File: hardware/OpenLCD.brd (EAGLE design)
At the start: 45.7 x 30.5 mm, 42 parts, among them Q1 PNP-500mA, Q2 PNP-500mA, Q3 PNP-500mA, U1 ATMEGA328P_TQFP, U2 4BIT-RGB, U3 MIC5205-ADJ, Y2 8MHz

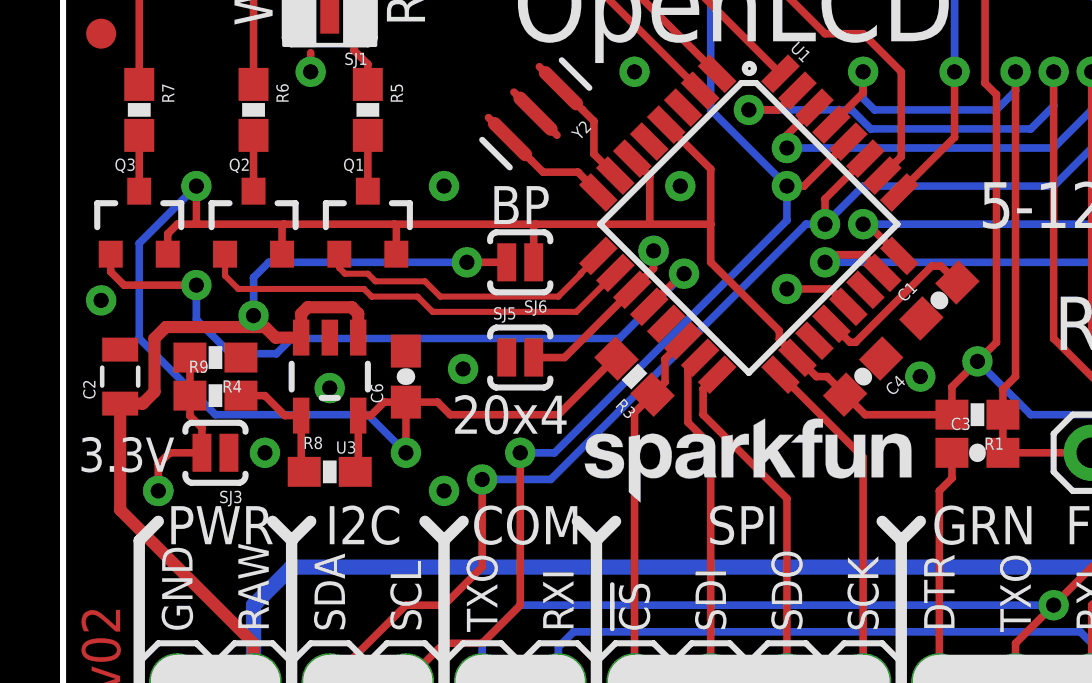
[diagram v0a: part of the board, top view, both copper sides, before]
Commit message: Connected blue backlight control pin to PWM on ATmega
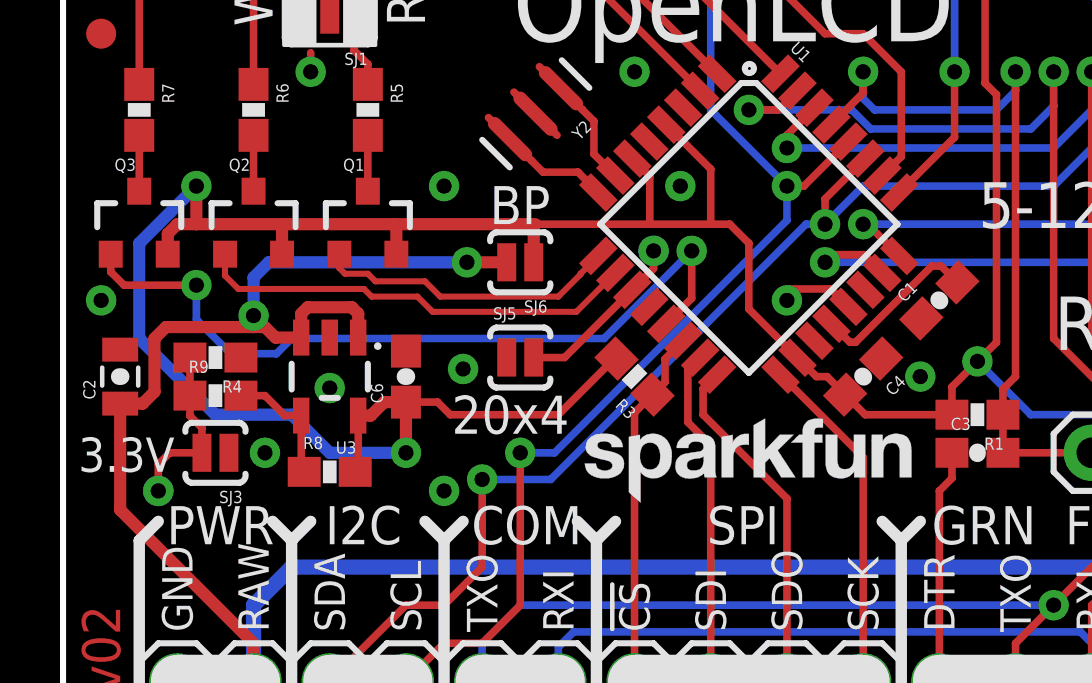
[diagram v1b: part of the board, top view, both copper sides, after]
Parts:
- C2: value 1.0uF/25V -> 1.0uF; device SparkFun-Capacitors:0805 -> SparkFun-Capacitors:0805-CAP
- JP3: value JST -> 3-PIN SMD
- U3: value MIC5205-ADJ -> ADJ
- Y2: value 8MHz -> 8MHZ
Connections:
- removed net CONTRAST: U1.13
- net BL-B: now also U1.13; no longer U1.12
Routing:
- net BL-B: track 24.2 -> 26.0 mm

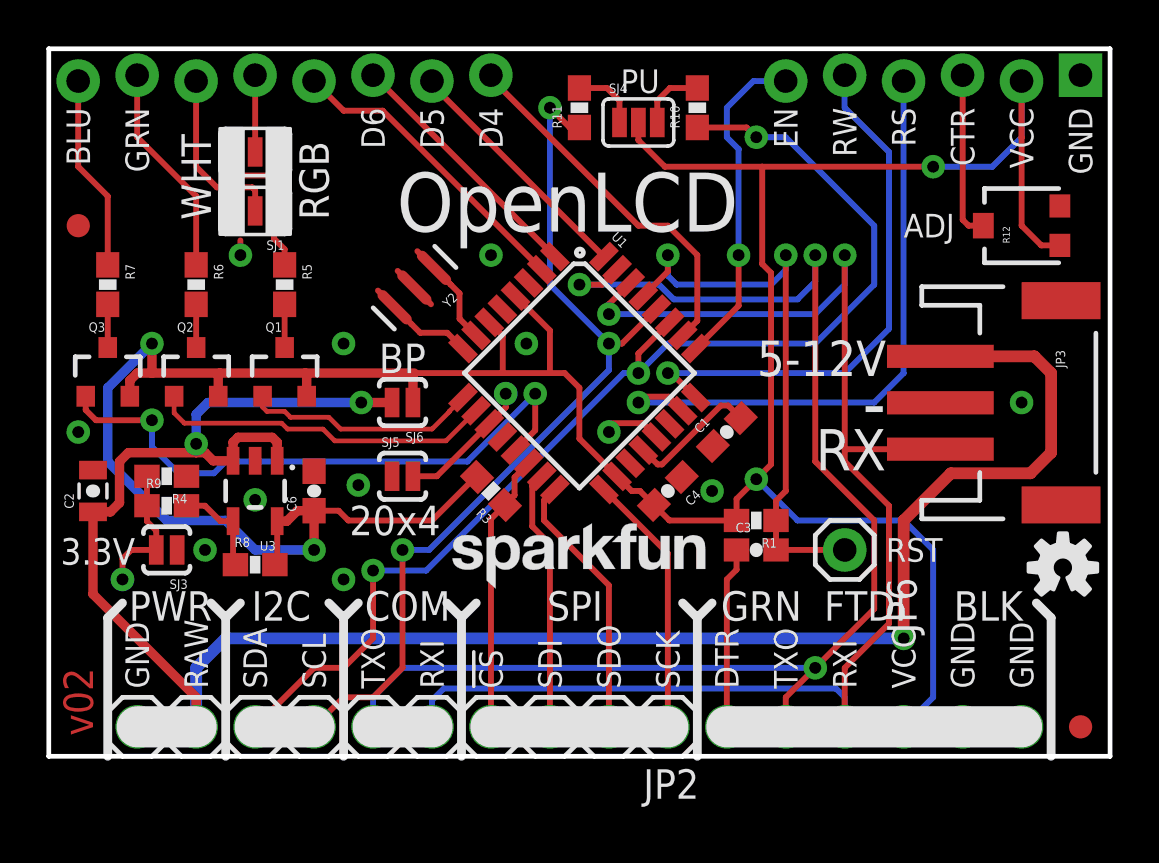
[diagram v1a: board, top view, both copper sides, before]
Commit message: Added MCP4725 for contrast control. Changed to 10uF tantulum.
We're going to try using the internal band gap reference for temp
control and modify the contrast based on that temp. We'll see if it
works...
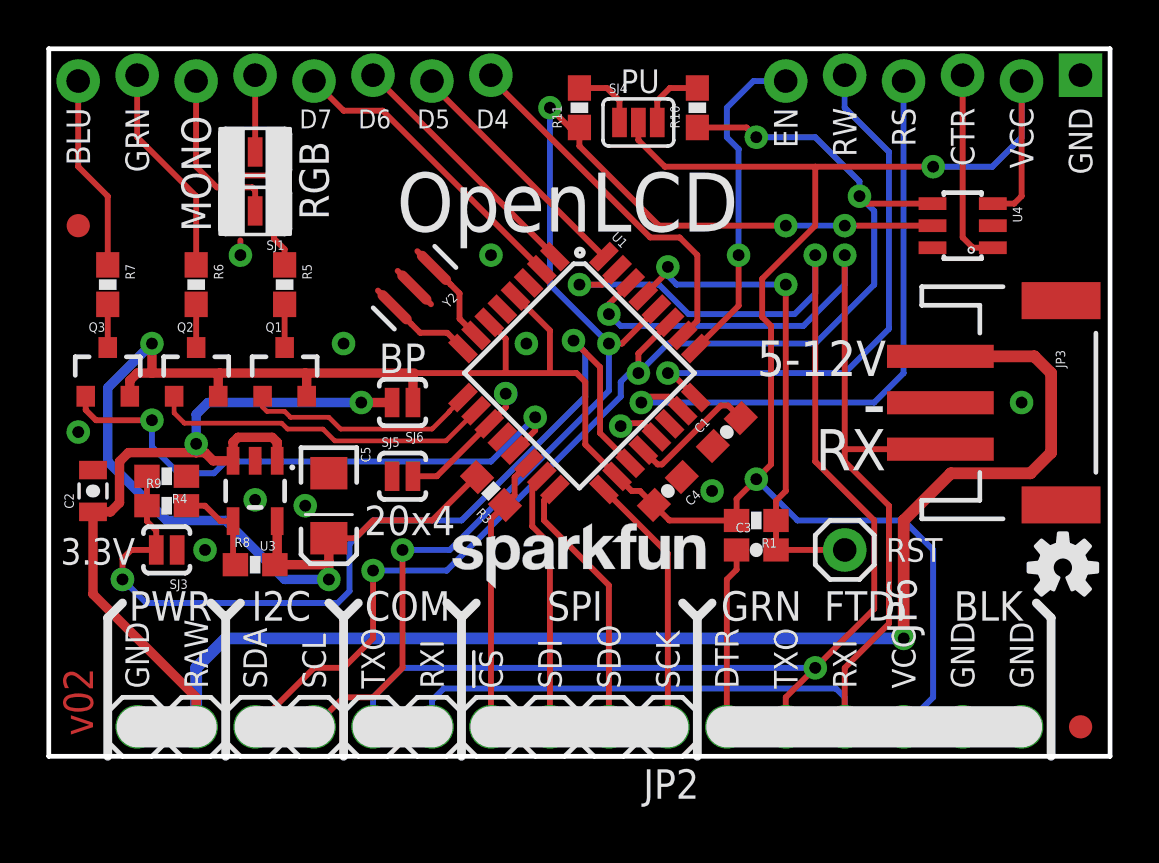
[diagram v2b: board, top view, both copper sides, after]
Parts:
- removed C6: 2.2uF, SparkFun-Capacitors:0603-CAP
- removed R12: 10k, SparkFun-Electromechanical:TRIMPOT-3MM
- added C5: 10uF, SparkFun-Capacitors:EIA3216
- added U4: MCP4725, SparkFun-AnalogIC:SOT23-6
- C2: value 1.0uF -> 1.0uF/25V
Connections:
- net A-RED/WHITE renamed MONO/RED
- removed net 3.3V_CTRL: R4.2, R9.1, SJ3.2, TP1.P$1
- removed net N$8: R12.2, U2.3
- new net 3V-JUMPER: R4.2, R9.1, SJ3.2, TP1.P$1, U1.19
- new net CONTRAST: U2.3, U4.1
- net GND: now also C5.C, U4.2, U4.6; no longer C6.2, R12.3
- net SCL: now also U4.5
- net SDA: now also U4.4
- net VCC: now also C5.A, U4.3; no longer C6.1, R12.1
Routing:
- net 3V-JUMPER: track 0.00 -> 40.0 mm, vias 0 -> 2
- net SCL: track 38.7 -> 56.6 mm, vias 3 -> 5
- net CONTRAST: track 0.00 -> 8.48 mm
- net N$8: track 7.23 -> 0.00 mm
- net 3.3V_CTRL: track 5.84 -> 0.00 mm, vias 1 -> 0
- net SDA: track 50.9 -> 55.3 mm, vias 3 -> 4
- net RST: track 25.1 -> 21.9 mm
- net BL-B: track 26.0 -> 24.5 mm
- net GND: track 3.31 -> 2.47 mm, vias 12 -> 11
- net TXO: track 57.6 -> 58.4 mm
- net VCC: track 133.5 -> 134.3 mm
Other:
- board text added: "D7"
- board text added: "MONO"
- board text added: "This side towards LCD"
- board text removed: "ADJ"
- board text removed: "WHT"

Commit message: Fixes for issue #4.
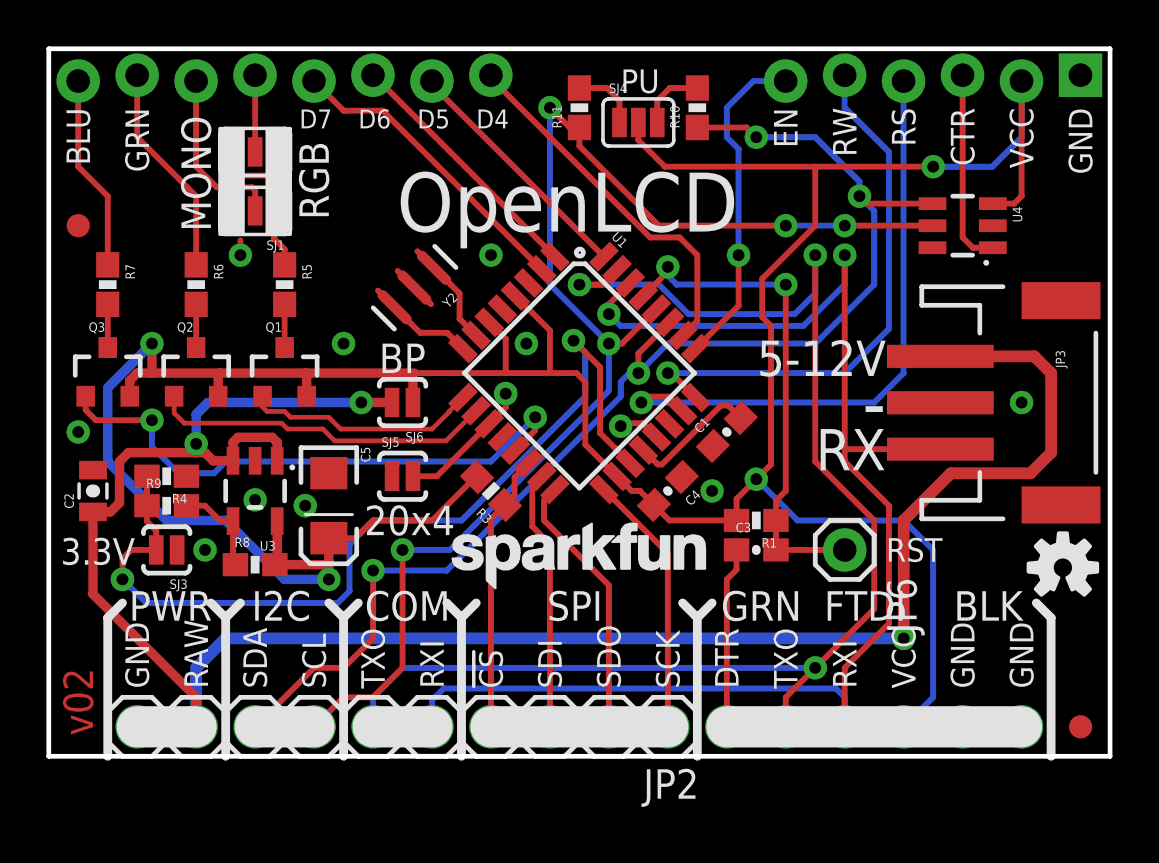
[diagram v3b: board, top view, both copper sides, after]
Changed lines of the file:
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@@
 <layer number="47" name="Measures" color="7" fill="1" visible="no" active="yes"/>
 <layer number="48" name="Document" color="7" fill="1" visible="no" active="yes"/>
-<layer number="49" name="Reference" color="7" fill="1" visible="yes" active="yes"/>
+<layer number="49" name="Reference" color="7" fill="1" visible="no" active="yes"/>
 <layer number="50" name="dxf" color="7" fill="1" visible="no" active="yes"/>
 <layer number="51" name="tDocu" color="6" fill="1" visible="yes" active="yes"/>
@@
 <layer number="112" name="tSilk" color="7" fill="1" visible="no" active="yes"/>
 <layer number="113" name="IDFDebug" color="7" fill="1" visible="no" active="yes"/>
+<layer number="114" name="Badge_Outline" color="7" fill="1" visible="yes" active="yes"/>
+<layer number="115" name="ReferenceISLANDS" color="7" fill="1" visible="yes" active="yes"/>
 <layer number="116" name="Patch_BOT" color="9" fill="4" visible="no" active="yes"/>
 <layer number="118" name="Rect_Pads" color="7" fill="1" visible="no" active="yes"/>
@@
 </class>
 </classes>
-<designrules name="default *">
-<description language="en">&lt;b&gt;EAGLE Design Rules&lt;/b&gt;
+<designrules name="SparkFun-2-layer-STANDARD *">
+<description language="en">&lt;b&gt;SparkFun 2 Layer Design Rule Checks - STANDARD/TIGHT/FAB-LIMIT&lt;/b&gt;
 &lt;p&gt;
-The default Design Rules have been set to cover
-a wide range of applications. Your particular design
-may have different requirements, so please make the
-necessary adjustments and save your customized
-design rules under a new name.</description>
+These rules have been curated by SparkFuns DFM commitee. After doing much research, communicating with our multiple fab houses, and getting quotes of various designs, we have compiled three DRU files.
+&lt;p&gt;
+&lt;b&gt;STANDARD:&lt;/b&gt; This is more of a &quot;best case scenario&quot; set of limitations. If your design has the space, and/or you have the time to work within these parameters, please do. Larger trace width and clearance makes for easier visual inspection of the PCB while troubleshooting (useful in production and to the end user). It also allows for better ability to hack a trace (if you are crazy enough to scrape away the mask and solder to a trace). Another thing to keep in mind is that more metal is just more robust.
+&lt;p&gt;
+&lt;b&gt;TIGHT:&lt;/b&gt; This is where cost comes into play. We have found that most fab houses begin to add extra charges when you go smaller than these specs. In some cases, going to less than 15 mil trace can increase the cost by 10%. (This is why we have set the min drill on this DRU to 15 mil) Same story for traces thinner than 7 mil. To avoid those extra charges, then stay within the rules of this DRU.
+&lt;p&gt;
+&lt;b&gt;FAB-LIMIT:&lt;/b&gt; These set of rules are at the very limit of most fab houses capabilities. You will pay more for these specs, and it should be used on designs that have a darned good reason to need 4 mil vias and 4 mil traces.
+&lt;p&gt;
+**NOTE Clearance, Distance, Sizes, and Restring are all set to different limits in each of these three DRU files. Please compare the files within the CAM job editor window of eagle to see all the numbers.
+&lt;p&gt;
+***NOTE, Please set your Net Classes to default (0mil for all settings), so that it won't effect the DRC when you run it with these settings.</description>
 <param name="layerSetup" value="(1*16)"/>
 <param name="mtCopper" value="0.035mm 0.035mm 0.035mm 0.035mm 0.035mm 0.035mm 0.035mm 0.035mm 0.035mm 0.035mm 0.035mm 0.035mm 0.035mm 0.035mm 0.035mm 0.035mm"/>
@@
 <param name="mdViaViaSameLayer" value="8mil"/>
 <param name="mnLayersViaInSmd" value="2"/>
-<param name="mdCopperDimension" value="10mil"/>
+<param name="mdCopperDimension" value="8mil"/>
 <param name="mdDrill" value="8mil"/>
 <param name="mdSmdStop" value="0mil"/>
@@
 <param name="rvMicroViaOuter" value="0.25"/>
 <param name="rvMicroViaInner" value="0.25"/>
-<param name="rlMinPadTop" value="12mil"/>
+<param name="rlMinPadTop" value="10mil"/>
 <param name="rlMaxPadTop" value="20mil"/>
 <param name="rlMinPadInner" value="10mil"/>
 <param name="rlMaxPadInner" value="20mil"/>
-<param name="rlMinPadBottom" value="12mil"/>
+<param name="rlMinPadBottom" value="10mil"/>
 <param name="rlMaxPadBottom" value="20mil"/>
 <param name="rlMinViaOuter" value="10mil"/>
@@
 <contactref element="SJ5" pad="1"/>
 <via x="1.27" y="13.97" extent="1-16" drill="0.508"/>
-<contactref element="U3" pad="2"/>
 <contactref element="SJ3" pad="1"/>
 <contactref element="R4" pad="1"/>
@@
 <wire x1="25.584684375" y1="14.351" x2="24.765" y2="14.351" width="0.254" layer="1"/>
 <wire x1="24.765" y1="14.351" x2="24.638" y2="14.224" width="0.254" layer="1"/>
+<contactref element="U3" pad="2"/>
 </signal>
 <signal name="RST">
@@
 <wire x1="42.291" y1="12.192" x2="43.18" y2="13.081" width="0.508" layer="1"/>
 <contactref element="U3" pad="1"/>
-<contactref element="U3" pad="3"/>
 <contactref element="C2" pad="1"/>
 <wire x1="6.35" y1="2.54" x2="1.905" y2="6.985" width="0.4064" layer="1"/>
 <wire x1="1.905" y1="10.53" x2="1.905" y2="6.985" width="0.4064" layer="1"/>
-<wire x1="7.94" y1="12.7301" x2="7.94" y2="13.528" width="0.4064" layer="1"/>
 <wire x1="9.84" y1="12.7301" x2="9.84" y2="13.528" width="0.4064" layer="1"/>
 <wire x1="1.905" y1="10.53" x2="2.656" y2="10.53" width="0.4064" layer="1"/>
@@
 <wire x1="6.35" y1="13.081" x2="6.731" y2="13.081" width="0.4064" layer="1"/>
 <wire x1="6.731" y1="13.081" x2="7.0819" y2="12.7301" width="0.4064" layer="1"/>
-<wire x1="7.94" y1="12.7301" x2="7.0819" y2="12.7301" width="0.4064" layer="1"/>
 <wire x1="9.6266" y1="13.7414" x2="8.1534" y2="13.7414" width="0.4064" layer="1"/>
 <wire x1="7.94" y1="13.528" x2="8.1534" y2="13.7414" width="0.4064" layer="1"/>
@@
 <via x="6.35" y="13.462" extent="1-16" drill="0.508"/>
 <wire x1="6.35" y1="13.462" x2="6.35" y2="13.081" width="0.4064" layer="1"/>
+<contactref element="U3" pad="3"/>
+<wire x1="7.94" y1="13.528" x2="7.94" y2="12.7301" width="0.4064" layer="1"/>
+<wire x1="7.0819" y1="12.7301" x2="7.94" y2="12.7301" width="0.4064" layer="1"/>
 </signal>
 <signal name="SDO">

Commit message: Fixes for issue #4.
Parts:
- U3: value ADJ -> MIC5205-ADJ
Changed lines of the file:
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@@
 <element name="SJ3" library="SparkFun-Passives" package="PAD-JUMPER-2-NO_YES_SILK" value="3.3V" x="5.08" y="8.89" rot="R180"/>
 <element name="SJ5" library="SparkFun-Passives" package="PAD-JUMPER-2-NO_YES_SILK" value="Size" x="15.24" y="12.065"/>
-<element name="U3" library="SparkFun-PowerIC" package="SOT23-5" value="ADJ" x="8.89" y="11.43" rot="R180">
+<element name="U3" library="SparkFun-PowerIC" package="SOT23-5" value="MIC5205-ADJ" x="8.89" y="11.43" rot="R180">
 <attribute name="PROD_ID" value="VREG-12594" x="8.89" y="11.43" size="1.27" layer="27" font="vector" ratio="15" rot="R180" display="off"/>
 </element>

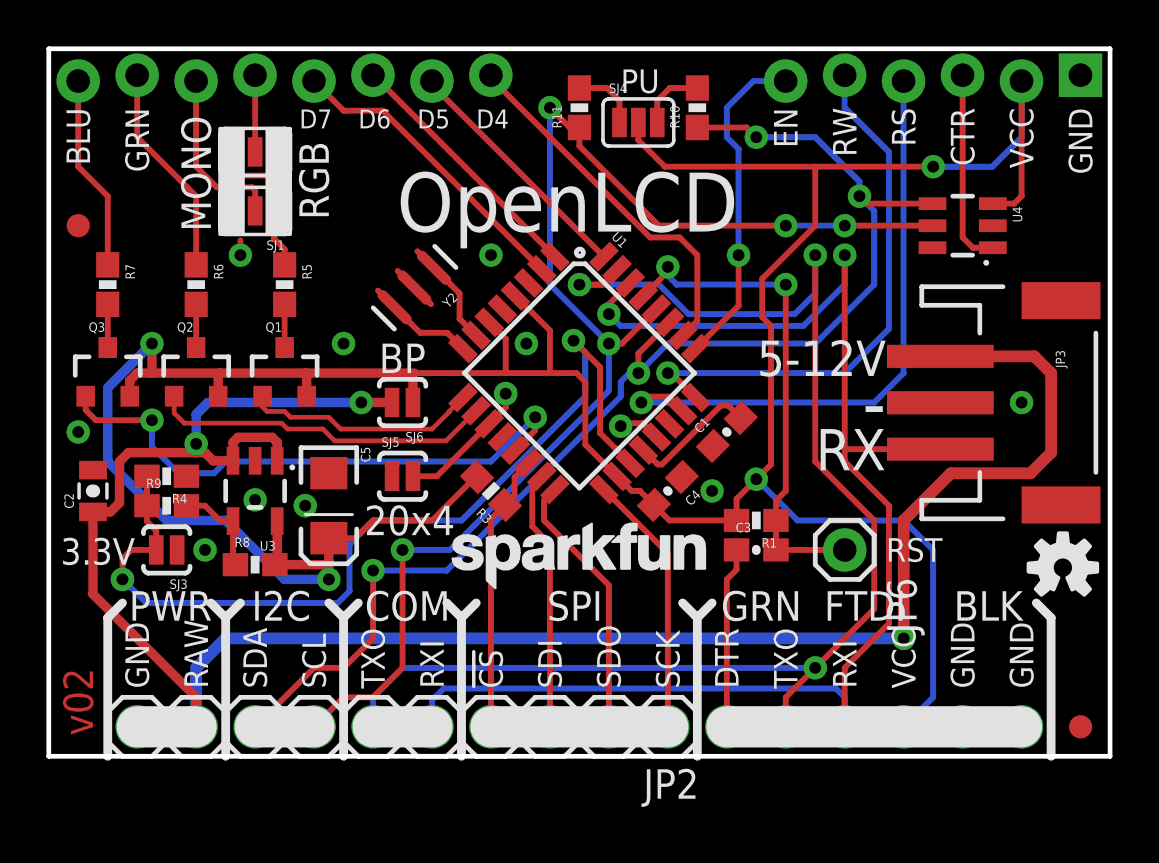
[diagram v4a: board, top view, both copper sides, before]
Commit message: Adding EEPROM support for custom chars. Fixing trace/space issue #4.
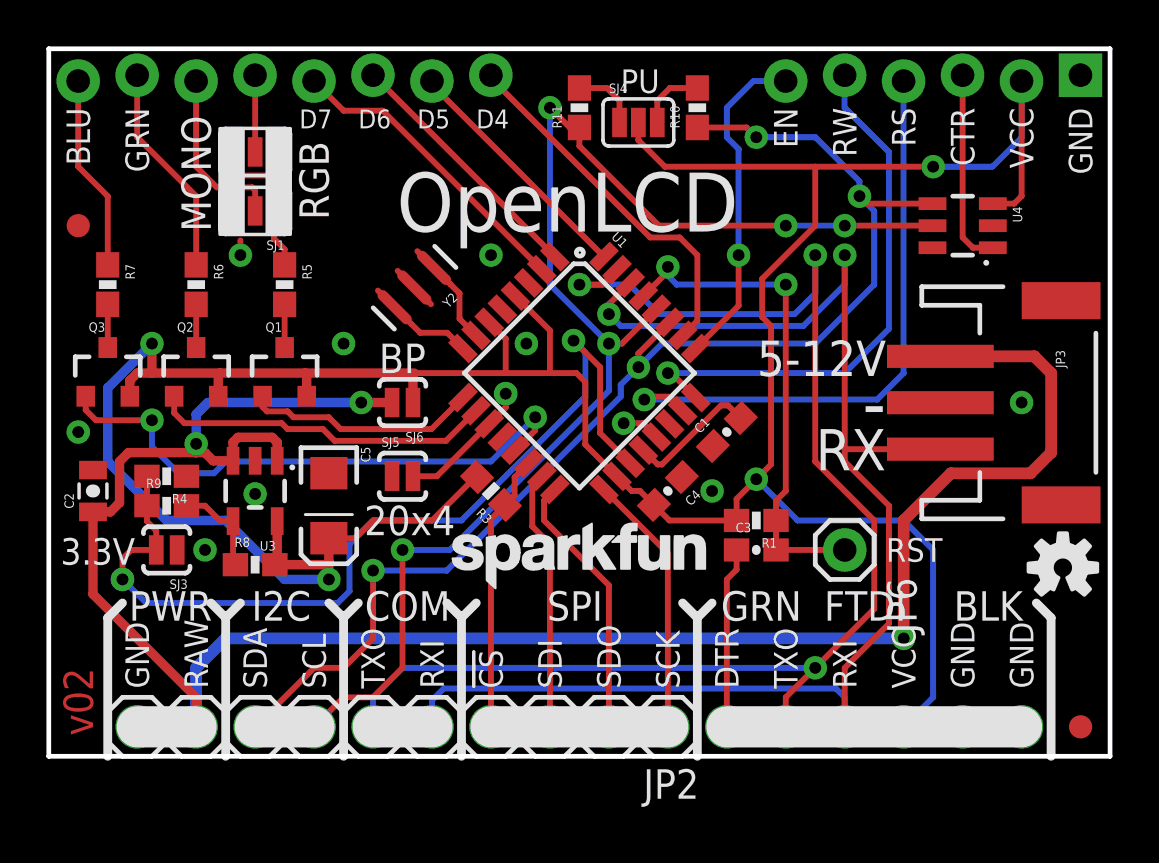
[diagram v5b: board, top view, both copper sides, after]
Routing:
- net GND: track 2.47 -> 2.29 mm, vias 11 -> 10
